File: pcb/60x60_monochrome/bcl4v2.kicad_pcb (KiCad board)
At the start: 2 copper layers, 60 x 60 mm, 51 parts, among them J1 Conn_01x05, J10 Conn_01x01_Female, J11 Conn_01x01_Female, J12 Conn_01x01_Female, J13 Conn_01x01_Female, J14 Conn_01x02, J15 Conn_01x04, J2 Conn_01x05, J3 USB_OTG, J4 Conn_01x05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

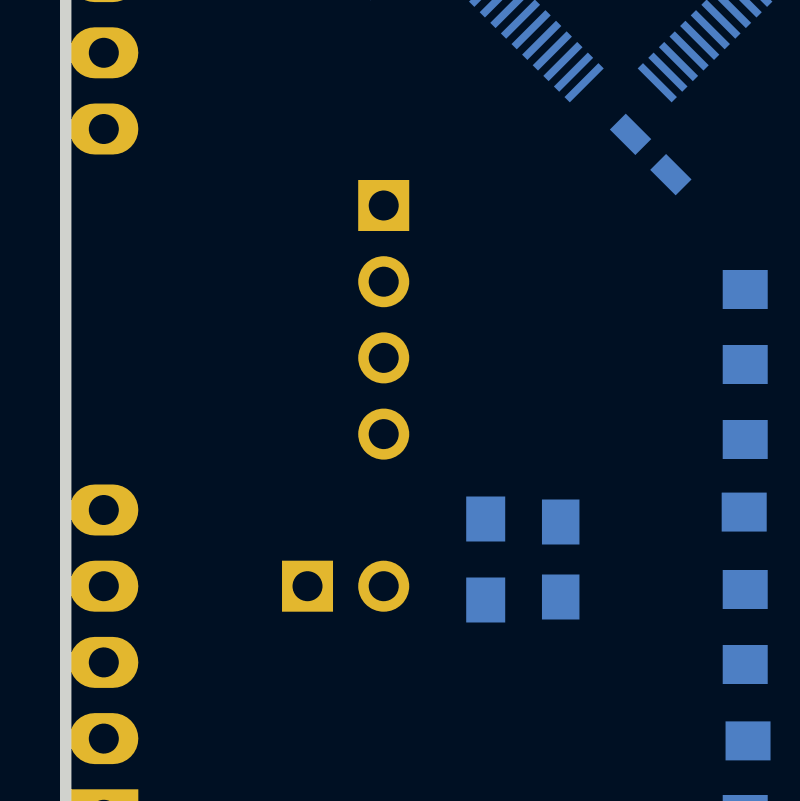
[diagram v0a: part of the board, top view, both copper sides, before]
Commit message: - make the headers better solderable
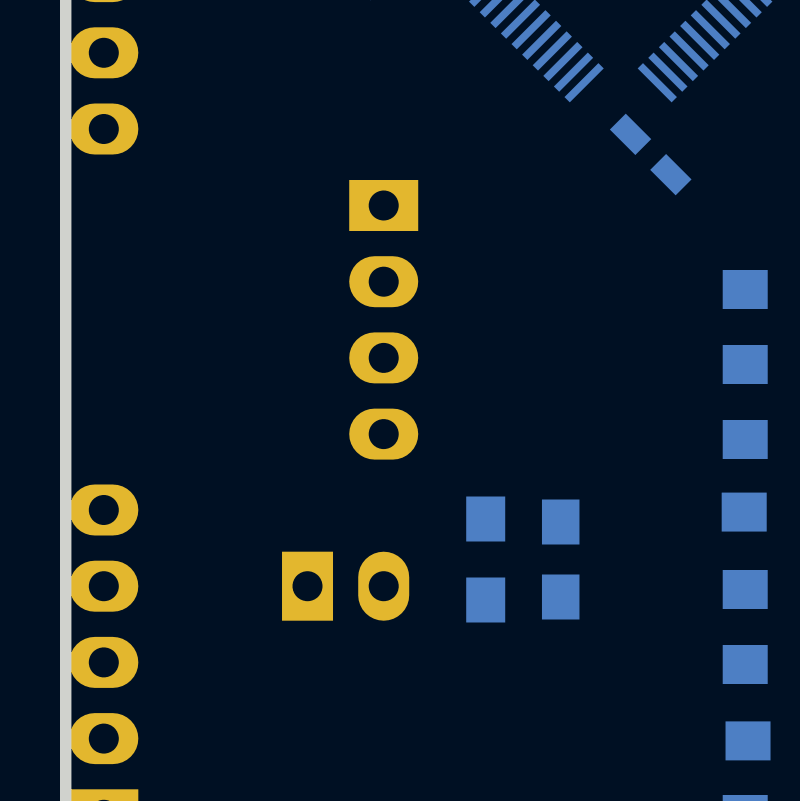
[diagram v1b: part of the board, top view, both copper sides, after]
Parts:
- J14: footprint Pin_Headers:Pin_Header_Angled_1x02_Pitch2.54mm -> kicad_libraries_new:badger_Pin_Hdr_1x02_2.54mm_angled_handsolder
- J15: footprint Pin_Headers:Pin_Header_Angled_1x04_Pitch2.54mm -> kicad_libraries_new:badger_Pin_Hdr_1x04_2.54mm_angled_handsolder

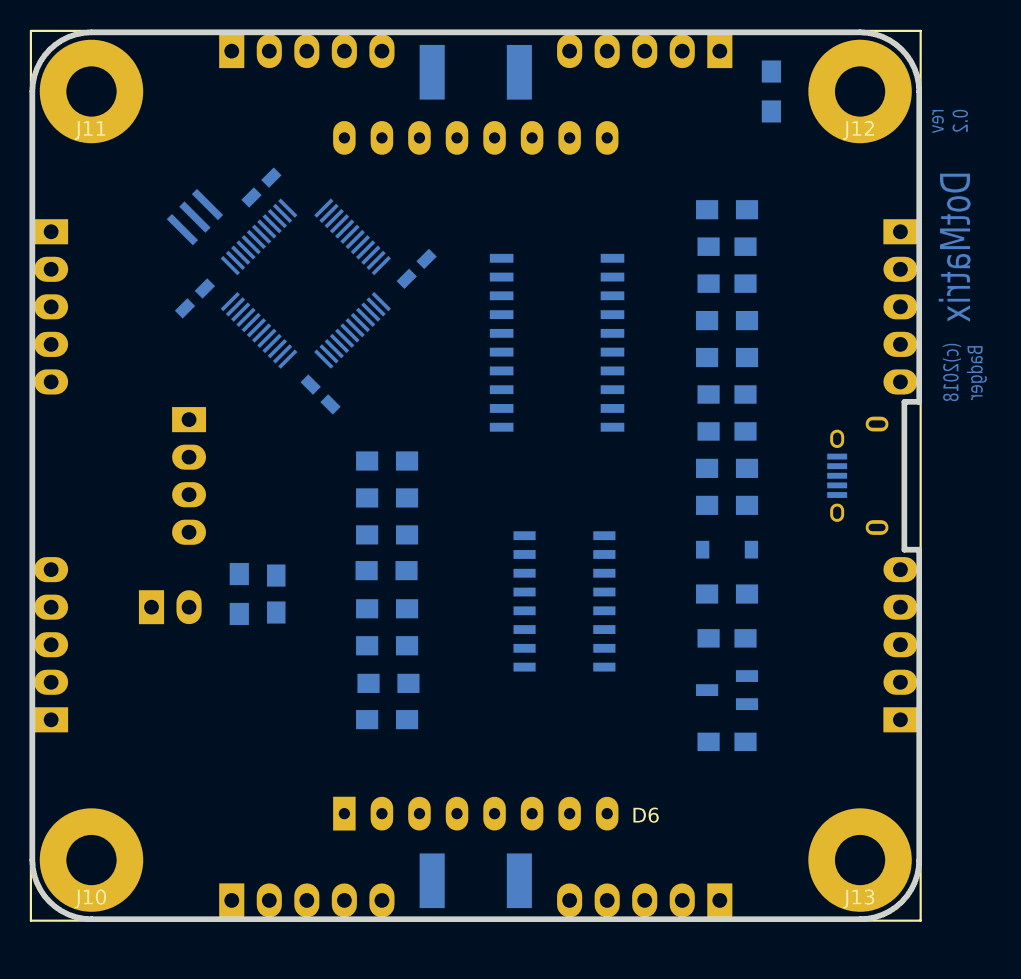
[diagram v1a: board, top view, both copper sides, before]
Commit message: - add pins to the sheets, add reset/boot circuit
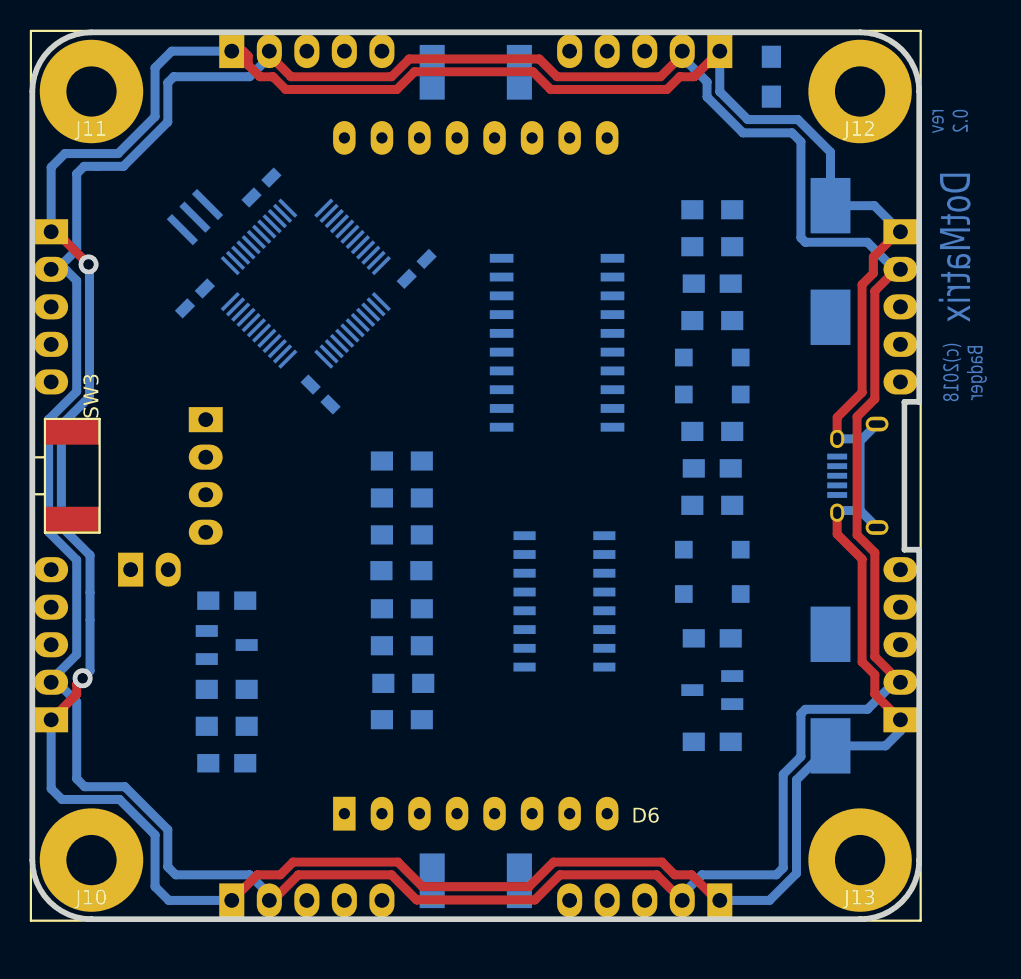
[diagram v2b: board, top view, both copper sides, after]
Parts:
- removed C5: 100n, Capacitors_SMD:C_0805_HandSoldering
- removed R15: 10k, Resistors_SMD:R_0805_HandSoldering
- added C10: 4u7, Capacitors_SMD:C_0805_HandSoldering, B.Cu at (83.2, 119.5)
- added C11: 100n, Capacitors_SMD:C_0805_HandSoldering, B.Cu at (83.2, 108.5)
- added C12: 220u, Capacitors_Tantalum_SMD:CP_Tantalum_Case-V_EIA-7343-20_Hand, B.Cu at (124.0, 85.5)
- added C13: 220u, Capacitors_Tantalum_SMD:CP_Tantalum_Case-V_EIA-7343-20_Hand, B.Cu at (124.0, 114.5)
- added Q1: BSS138, kicad_libraries_new:badger_SOT-23_handsolder, B.Cu at (83.2, 111.5)
- added R16: 820k, Resistors_SMD:R_0805_HandSoldering, B.Cu at (83.2, 117.0)
- added R3: R, Resistors_SMD:R_0805_HandSoldering, B.Cu at (95.0, 99.0)
- added SW3: SW_Push, kicad_libraries_new:badger_smd_button_KSS231G, F.Cu at (72.7, 100.0)
- C1, C3: value 2u2 -> 4u7
- D1, D2, D4: footprint LEDs:LED_0805_HandSoldering -> kicad_libraries_new:badger_D_SOD-123_hand
- D3: footprint Diodes_SMD:D_SOD-123 -> kicad_libraries_new:badger_D_SOD-123_hand
- R1, R4: footprint Capacitors_SMD:C_0805_HandSoldering -> Resistors_SMD:R_0805_HandSoldering
- R13: value R -> 10k
- moved R5 20.0 mm to (116.0, 82.0)
- moved R13 18.9 mm to (83.2, 114.5), turned to 180 degrees
- moved J14 2.91 mm to (76.7, 106.3)
- moved C2 2.69 mm to (116.0, 87.0)
- moved C4 2.69 mm to (116.0, 99.5)
- moved D1 2.69 mm to (116.0, 92.0)
- moved D2 2.69 mm to (116.0, 94.5)
- moved R1 2.69 mm to (116.0, 89.5)
- moved R14 2.69 mm to (116.0, 84.5)
- moved R2 2.69 mm to (116.0, 102.0)
- moved R4 2.69 mm to (116.0, 97.0)
- moved J15 1.13 mm to (81.7, 96.2)
- moved C1 1.00 mm to (116.0, 111.0)
- moved C3 1.00 mm to (116.0, 118.0)
- moved D3 1.00 mm to (116.0, 105.0)
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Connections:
- net /OUT_A0 renamed /LED_matrix/OUT_A0
- net /OUT_A1 renamed /LED_matrix/OUT_A1
- net /OUT_A2 renamed /LED_matrix/OUT_A2
- net /OUT_A3 renamed /LED_matrix/OUT_A3
- net /OUT_A4 renamed /LED_matrix/OUT_A4
- net /OUT_A5 renamed /LED_matrix/OUT_A5
- net /OUT_A6 renamed /LED_matrix/OUT_A6
- net /OUT_A7 renamed /LED_matrix/OUT_A7
- D6 pad 10: /OUT_C4 -> /LED_matrix/OUT_C4
- D6 pad 11: /OUT_C6 -> /LED_matrix/OUT_C6
- D6 pad 13: /OUT_C1 -> /LED_matrix/OUT_C1
- D6 pad 15: /OUT_C7 -> /LED_matrix/OUT_C7
- D6 pad 16: /OUT_C8 -> /LED_matrix/OUT_C8
- D6 pad 3: /OUT_C2 -> /LED_matrix/OUT_C2
- D6 pad 4: /OUT_C3 -> /LED_matrix/OUT_C3
- D6 pad 6: /OUT_C5 -> /LED_matrix/OUT_C5
- J1 pad 3: /UART_TX4 -> /UART_RX4
- J3 pad 2: /USB_DM -> /USB_DP
- J3 pad 3: /USB_DP -> /USB_DM
- R10 pad 1: /OUT_C5 -> /LED_matrix/OUT_C6
- R10 pad 2: /C5 -> /LED_matrix/C6
- R11 pad 1: /OUT_C6 -> /LED_matrix/OUT_C7
- R11 pad 2: /C6 -> /LED_matrix/C7
- R12 pad 1: /OUT_C7 -> /LED_matrix/OUT_C8
- R12 pad 2: /C7 -> /LED_matrix/C8
- R13 pad 1: /OUT_C8 -> Net-(Q1-Pad1)
- R13 pad 2: /C8 -> GND
- R6 pad 1: /OUT_C1 -> /LED_matrix/OUT_C2
- R6 pad 2: /C1 -> /LED_matrix/C2
- R7 pad 1: /OUT_C2 -> /LED_matrix/OUT_C3
- R7 pad 2: /C2 -> /LED_matrix/C3
- R8 pad 1: /OUT_C3 -> /LED_matrix/OUT_C4
- R8 pad 2: /C3 -> /LED_matrix/C4
- R9 pad 1: /OUT_C4 -> /LED_matrix/OUT_C5
- R9 pad 2: /C4 -> /LED_matrix/C5
- U2 pad 10: /UART_TX4 -> /UART_RX4
- U3 pad 11: /C5 -> /LED_matrix/C5
- U3 pad 12: /C6 -> /LED_matrix/C6
- U3 pad 13: /C7 -> /LED_matrix/C7
- U3 pad 14: /C8 -> /LED_matrix/C8
- U3 pad 3: /C1 -> /LED_matrix/C1
- U3 pad 4: /C2 -> /LED_matrix/C2
- U3 pad 5: /C3 -> /LED_matrix/C3
- U3 pad 6: /C4 -> /LED_matrix/C4
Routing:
- net GND: track 0.00 -> 239.8 mm, vias 0 -> 2
- net VCC: track 0.00 -> 228.5 mm
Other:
- net class power: via_dia 0.9652 -> 1.3462

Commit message: - fix USB lines
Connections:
- J10 pad 1: (no net) -> Net-(J10-Pad1)
- J11 pad 1: (no net) -> Net-(J11-Pad1)
- J12 pad 1: (no net) -> Net-(J12-Pad1)
- J13 pad 1: (no net) -> Net-(J13-Pad1)
- J3 pad 2: /USB_DP -> /USB_D-
- J3 pad 3: /USB_DM -> /USB_D+
- J3 pad 4: (no net) -> Net-(J3-Pad4)
- U2 pad 20: (no net) -> Net-(U2-Pad20)
- U2 pad 32: /USB_DM -> /USB_D-
- U2 pad 33: /USB_DP -> /USB_D+
- U3 pad 9: (no net) -> Net-(U3-Pad9)
- U4 pad 1: (no net) -> Net-(U4-Pad1)
- U4 pad 20: (no net) -> Net-(U4-Pad20)

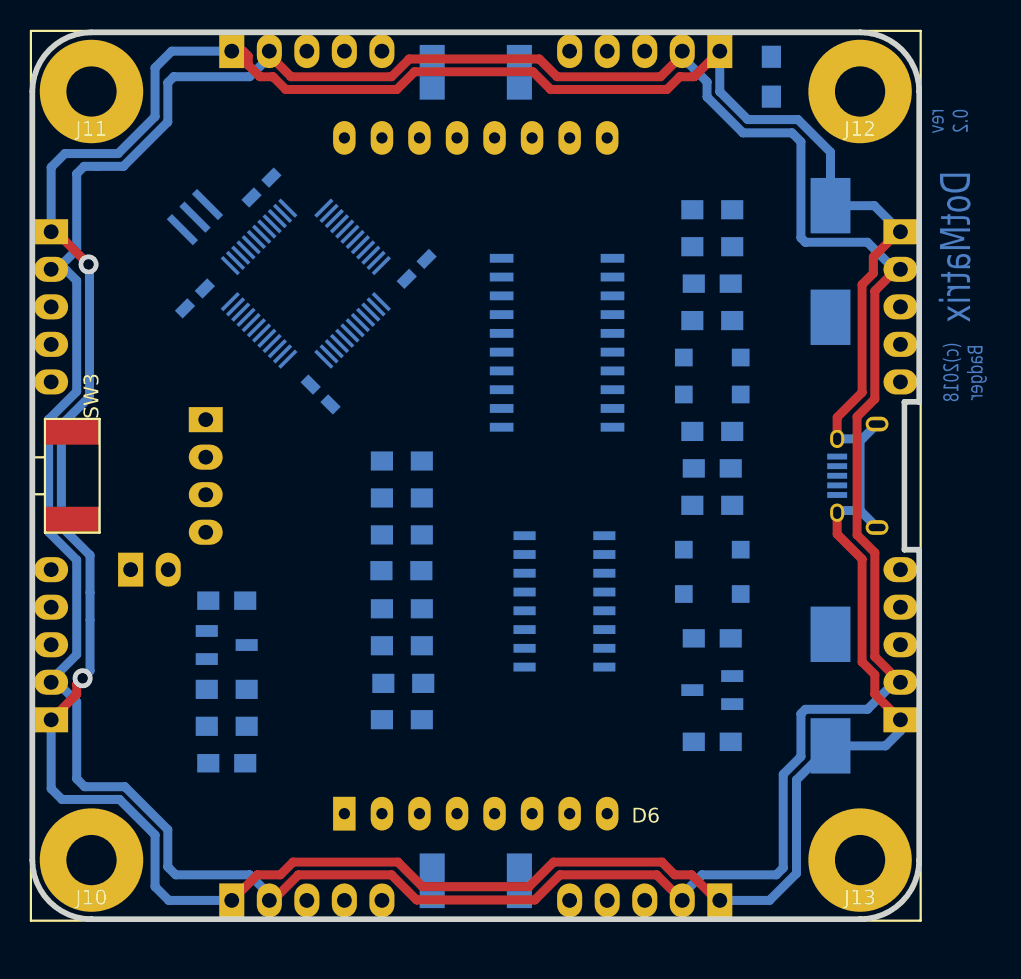
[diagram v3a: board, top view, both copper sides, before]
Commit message: - replaced protection LEDs with mosfet
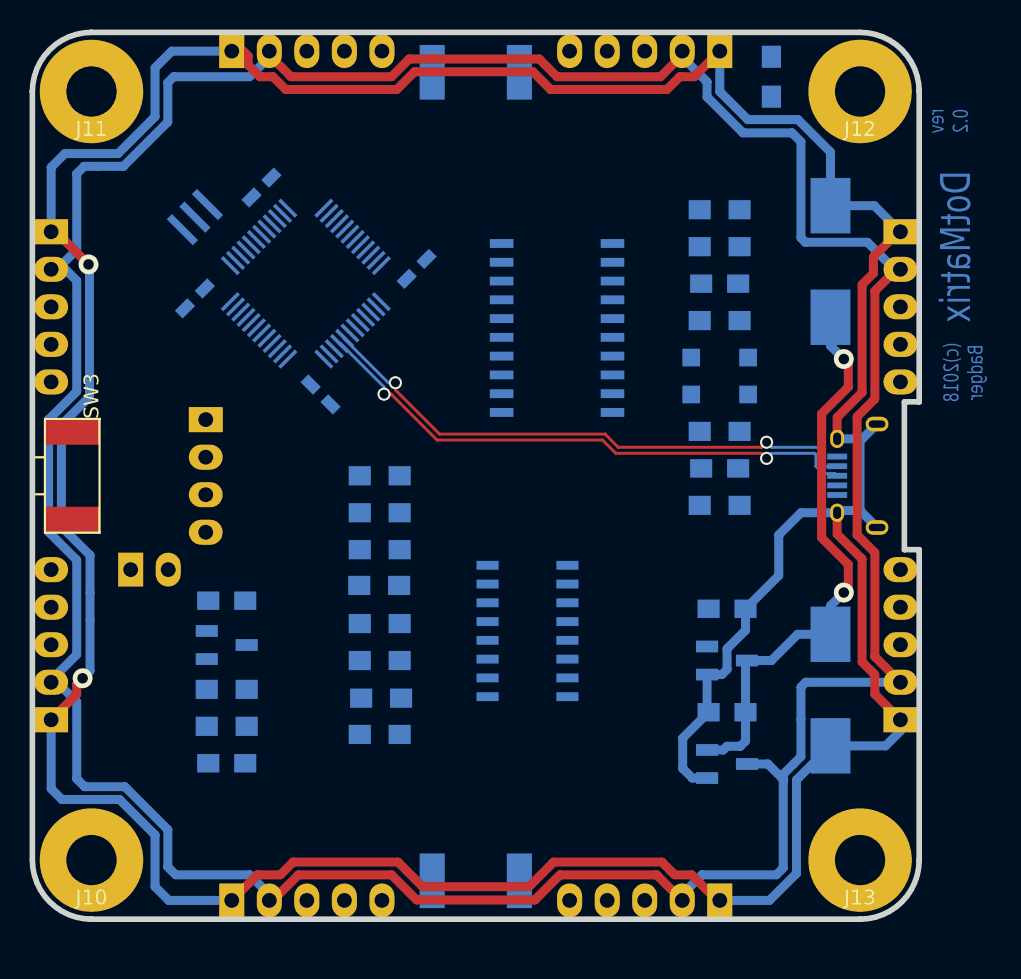
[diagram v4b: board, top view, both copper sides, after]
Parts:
- removed D3, D4: Shottky, kicad_libraries_new:badger_D_SOD-123_hand
- removed D6: LED_MATRIX_8x8, kicad_libraries_new:badger_LED_MATRIX_8x8_60.2mmx60.2mm
- added Q2: IRLML6402, kicad_libraries_new:badger_SOT-23_handsolder, B.Cu at (117.0, 119.5)
- moved C3 9.06 mm to (117.0, 109.0)
- moved C1 5.10 mm to (117.0, 116.0), turned to 180 degrees
- moved U3 3.20 mm to (103.5, 110.5)
- moved U1 2.24 mm to (117.0, 112.5), turned to 0 degrees
- moved R10 1.80 mm to (93.5, 107.4)
- moved R11 1.80 mm to (93.5, 105.0)
- moved R12 1.80 mm to (93.5, 102.5)
- moved R3 1.80 mm to (93.5, 100.0)
- moved R6 1.80 mm to (93.5, 117.5)
- moved R7 1.80 mm to (93.6, 115.0)
- moved R8 1.80 mm to (93.5, 112.5)
- moved R9 1.80 mm to (93.5, 110.0)
- moved U4 1.00 mm to (105.5, 90.0)
- moved C2 0.50 mm to (116.5, 87.0)
- moved C4 0.50 mm to (116.5, 99.5)
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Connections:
- J1 pad 3: /UART_RX4 -> /UART_TX4
- J1 pad 4: /IN1P -> /I2C_SDA
- J1 pad 5: /I2C_SDA -> /IN1P
- J10 pad 1: Net-(J10-Pad1) -> (no net)
- J11 pad 1: Net-(J11-Pad1) -> (no net)
- J12 pad 1: Net-(J12-Pad1) -> (no net)
- J13 pad 1: Net-(J13-Pad1) -> (no net)
- J2 pad 4: /BTN0 -> /I2C_SCL
- J2 pad 5: /I2C_SCL -> /BTN0
- J3 pad 1: Net-(D3-Pad2) -> +5V
- J3 pad 4: Net-(J3-Pad4) -> (no net)
- J4 pad 4: /IN0P -> /I2C_SCL
- J4 pad 5: /I2C_SCL -> /IN0P
- J5 pad 4: /BTN1 -> /I2C_SDA
- J5 pad 5: /I2C_SDA -> /BTN1
- J6 pad 4: /IN1P -> /I2C_SDA
- J6 pad 5: /I2C_SDA -> /IN1P
- J7 pad 4: /IN3 -> /I2C_SCL
- J7 pad 5: /I2C_SCL -> /IN3
- J8 pad 4: /IN0P -> /I2C_SCL
- J8 pad 5: /I2C_SCL -> /IN0P
- J9 pad 4: /IN2 -> /I2C_SDA
- J9 pad 5: /I2C_SDA -> /IN2
- U2 pad 10: /UART_RX4 -> /UART_TX4
- U2 pad 20: Net-(U2-Pad20) -> (no net)
- U3 pad 9: Net-(U3-Pad9) -> (no net)
- U4 pad 1: Net-(U4-Pad1) -> (no net)
- U4 pad 20: Net-(U4-Pad20) -> (no net)
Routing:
- net +5V: track 0.00 -> 39.6 mm, vias 0 -> 2
- net /USB_D+: track 0.00 -> 38.4 mm, vias 0 -> 2
- net /USB_D-: track 0.00 -> 38.0 mm, vias 0 -> 2
- net GND: track 239.8 -> 265.4 mm
- net VCC: track 228.5 -> 232.9 mm

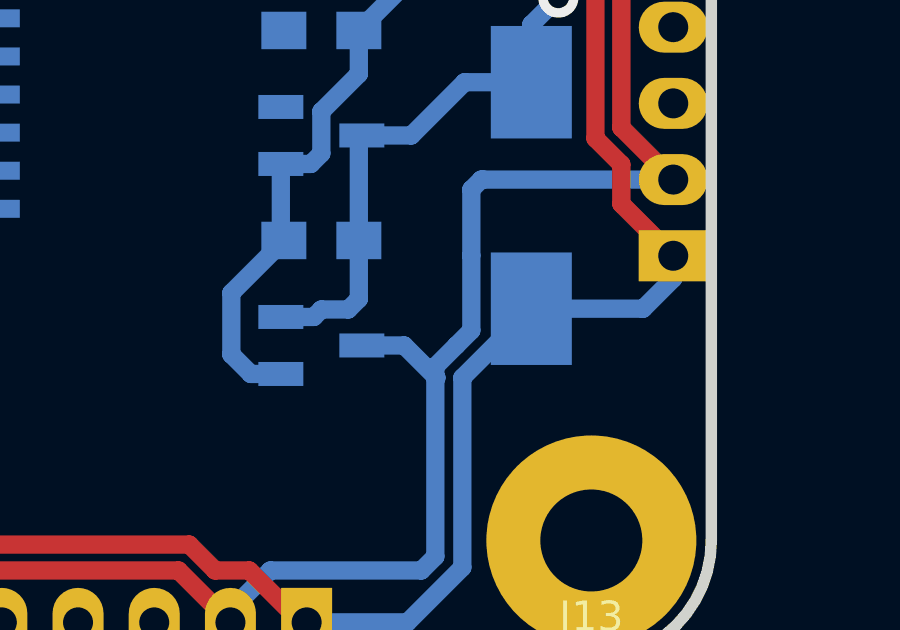
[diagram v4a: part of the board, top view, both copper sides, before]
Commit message: - pcb (hopefully) ready for first routing attempt
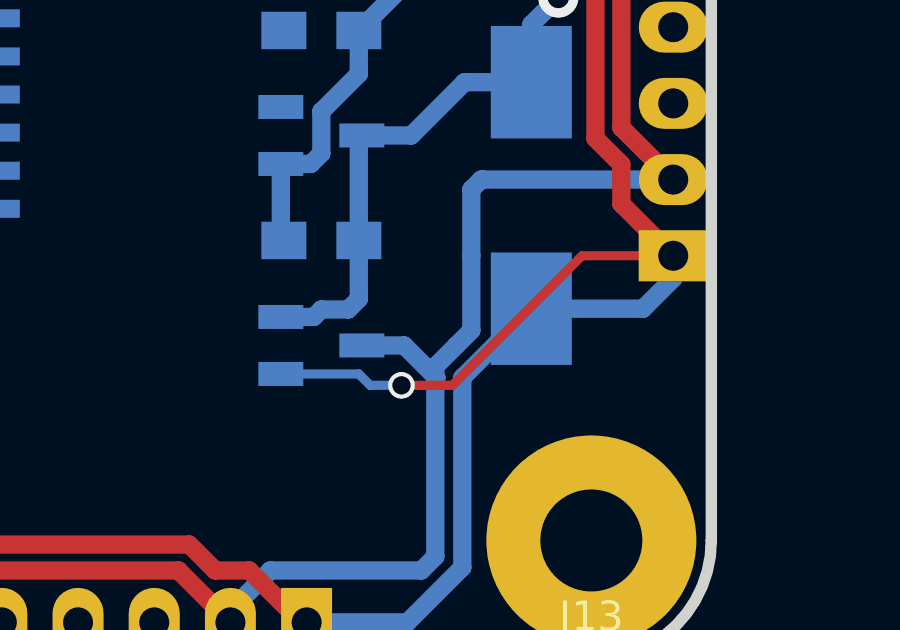
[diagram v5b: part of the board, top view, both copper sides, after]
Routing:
- net GND: track 265.4 -> 274.0 mm, vias 2 -> 3
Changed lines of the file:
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@@
     (thickness 1.6002)
     (drawings 24)
-    (tracks 259)
+    (tracks 262)
     (zones 0)
     (modules 55)
@@
     (arrow2b (pts (xy 100 96) (xy 101.126504 95.413579)))
   )
+  (segment (start 121.371258 120.828742) (end 125.69 116.51) (width 0.3048) (layer Front) (net 1))
+  (segment (start 125.69 116.51) (end 128.73 116.51) (width 0.3048) (layer Front) (net 1))
+  (segment (start 119.671258 120.828742) (end 121.371258 120.828742) (width 0.3048) (layer Front) (net 1))
+  (segment (start 118.25 120.45) (end 118.628742 120.828742) (width 0.3048) (layer Back) (net 1))
+  (segment (start 118.628742 120.828742) (end 119.671258 120.828742) (width 0.3048) (layer Back) (net 1))
+  (via (at 119.671258 120.828742) (size 0.889) (drill 0.6096) (layers Front Back) (net 1))
+  (segment (start 115.65 120.45) (end 118.25 120.45) (width 0.3048) (layer Back) (net 1))
   (segment (start 124.45 102.5) (end 122 102.5) (width 0.6096) (layer Back) (net 1))
   (segment (start 120.5 106.75) (end 118.25 109) (width 0.6096) (layer Back) (net 1))
   (segment (start 120.5 104) (end 120.5 106.75) (width 0.6096) (layer Back) (net 1))
   (segment (start 122 102.5) (end 120.5 104) (width 0.6096) (layer Back) (net 1))
-  (segment (start 115.65 120.45) (end 114.65 120.45) (width 0.6096) (layer Back) (net 1))
-  (segment (start 114 117.75) (end 115.75 116) (width 0.6096) (layer Back) (net 1))
-  (segment (start 114 119.8) (end 114 117.75) (width 0.6096) (layer Back) (net 1))
-  (segment (start 114.65 120.45) (end 114 119.8) (width 0.6096) (layer Back) (net 1))
   (segment (start 115.65 113.45) (end 115.65 115.9) (width 0.6096) (layer Back) (net 1))
   (segment (start 115.65 115.9) (end 115.75 116) (width 0.6096) (layer Back) (net 1))
